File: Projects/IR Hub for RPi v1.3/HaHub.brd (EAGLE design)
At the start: 65 x 56 mm, 39 parts, among them SW1 SPST_TACT-KMR2, SW2 SPST_TACT-KMR2, SW3 SPST_TACT-KMR2, T1 2N4401, T2 2N4401, T3 2N4401, T4 2N4401

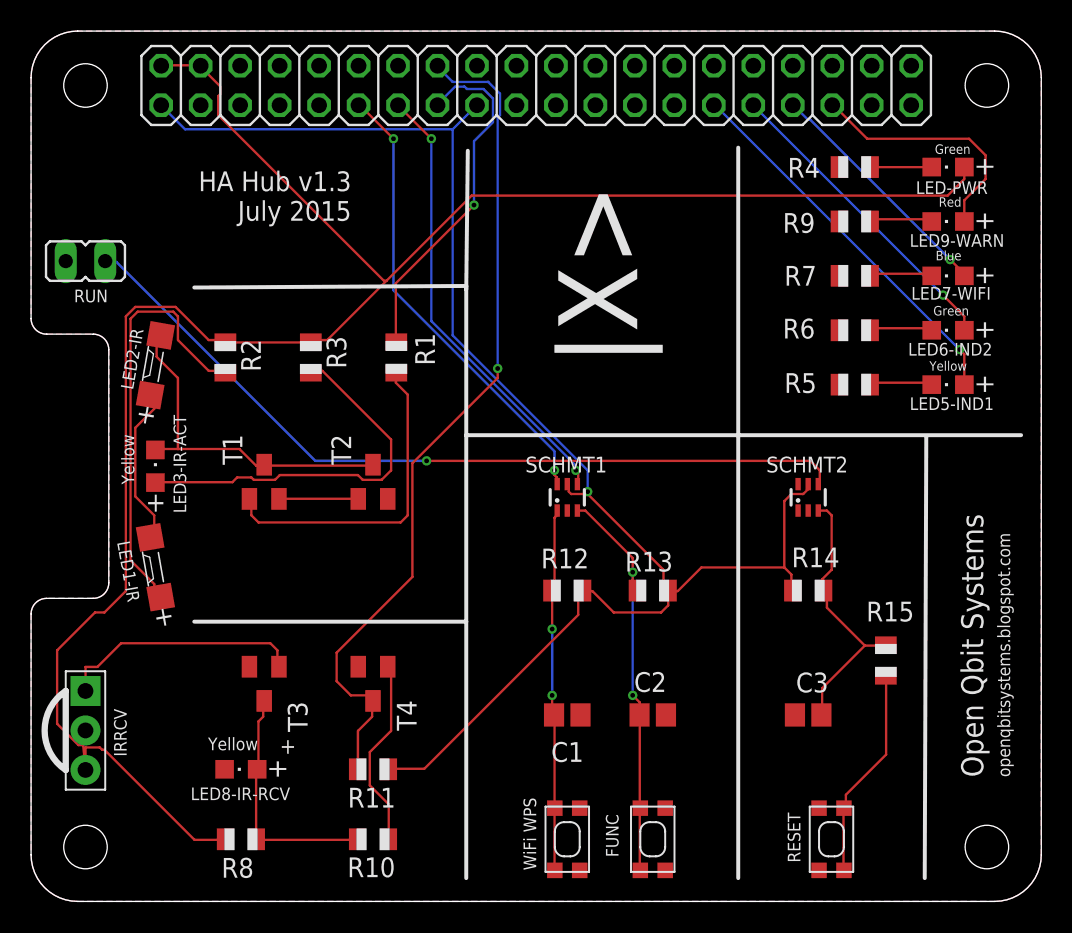
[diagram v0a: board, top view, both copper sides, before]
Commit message: Board layout changed
Removed the cutout in the board thus moved the IR emitters a bit
forward, avoiding the obstruction from the IRRCV when angled at 15deg.
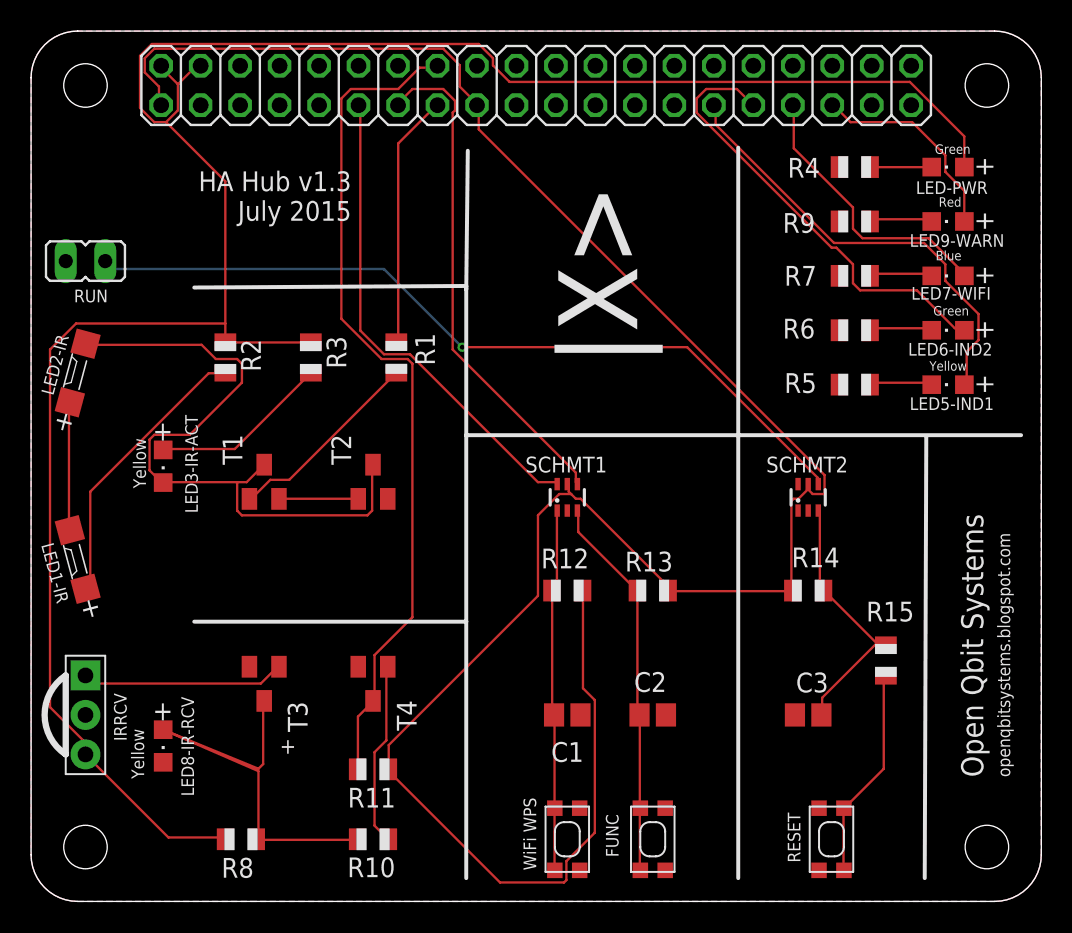
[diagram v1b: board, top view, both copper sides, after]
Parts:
- moved LED8-IR-RCV 5.22 mm to (8.50, 10.0), turned to 180 degrees
- moved LED1-IR 5.02 mm to (3.00, 22.0), turned to 195 degrees
- moved LED2-IR 5.02 mm to (3.00, 34.0), turned to 165 degrees
- moved IRRCV 1.00 mm to (3.50, 12.0)
- moved LED3-IR-ACT 0.50 mm to (8.50, 28.0), turned to 180 degrees
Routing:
- net +3V3: track 100.4 -> 146.0 mm, vias 1 -> 0
- net N$4: track 22.7 -> 43.2 mm
- net +5V: track 127.1 -> 141.4 mm
- net N$6: track 24.9 -> 11.6 mm
- net N$10: track 15.6 -> 28.8 mm
- net N$2: track 27.8 -> 18.2 mm
- net GPIO06: track 20.1 -> 29.1 mm, vias 1 -> 0
- net N$5: track 21.0 -> 12.8 mm
- net GPIO22: track 22.7 -> 16.4 mm, vias 1 -> 0
- net GPIO05: track 24.7 -> 28.9 mm, vias 1 -> 0
- net GPIO27: track 29.2 -> 32.5 mm, vias 2 -> 0
- net N$8: track 15.8 -> 13.1 mm
- net GPIO19: track 16.0 -> 13.4 mm
- net GPIO13: track 15.7 -> 18.1 mm, vias 1 -> 0
- net N$3: track 10.6 -> 8.27 mm
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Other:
- outline, holes or cut-outs redrawn
- board text added: "TODO DONE 1. Check the Schmitt debouncing on breadboard 2. Check both ICs wrt 74HC/74LV/... for 3.3V1. check the polarity of the IR LEDs 3. Add schmitt buffers for all the push buttons (create part) 4. ELIMINATED - Verify the Watchdog circuit 5. ELIMINATED - Will RPi gpio go in a state to allow disabling WD? 6. Ensure long push for RESET push button (cap and resistor values) 7. Move Power LED to 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"
- board text removed: "TODO 1. Check the Schmitt debouncing on breadboard 3. Check both ICs wrt 74HC/74LV/... for 3.3V DONE 1. check the polarity of the IR LEDs 2. Add schmitt buffers for all the push buttons (create part) 3. ELIMINATED - Verify the Watchdog circuit 4. ELIMINATED - Will RPi gpio go in a state to allow disabling WD? 5. Ensure long push for RESET push button (cap and resistor values) 6. Move Power LED to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"

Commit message: Changed v1.3 board 'via' drill size to 13mil. Plus some house keeping,
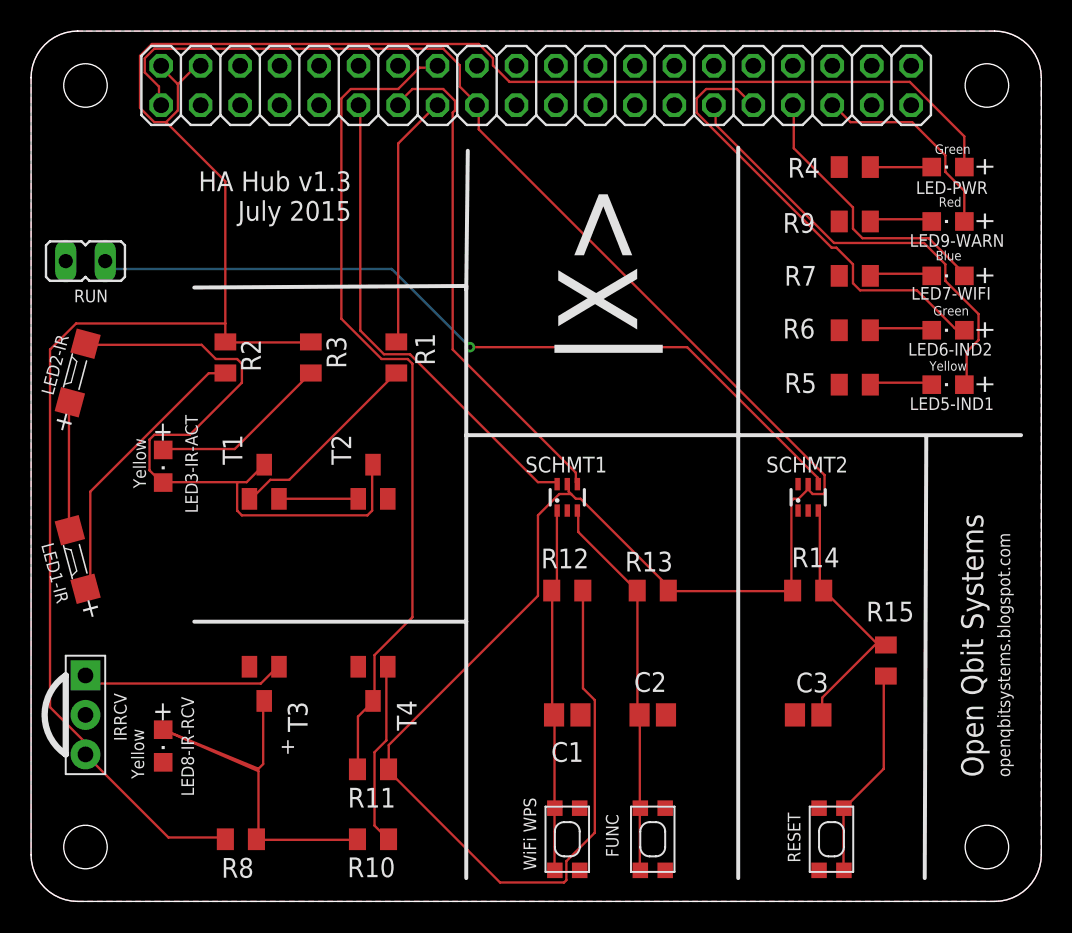
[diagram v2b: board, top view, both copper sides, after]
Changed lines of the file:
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@@
 <setting verticaltext="up"/>
 </settings>
-<grid distance="0.5" unitdist="mm" unit="mm" style="lines" multiple="1" display="yes" altdistance="0.25" altunitdist="mm" altunit="mm"/>
+<grid distance="19.6850394" unitdist="mil" unit="mil" style="lines" multiple="1" display="yes" altdistance="9.84251969" altunitdist="mil" altunit="mil"/>
 <layers>
 <layer number="1" name="Top" color="4" fill="1" visible="yes" active="yes"/>
@@
 <wire x1="45.5" y1="48.5" x2="45.5" y2="30" width="0.254" layer="25"/>
 <wire x1="63.7" y1="30" x2="28" y2="30" width="0.254" layer="25"/>
-<text x="-48.2222" y="19.964" size="1.016" layer="48">
+<text x="-4.964" y="2.7778" size="1.016" layer="48" rot="R90">
 TODO
 DONE
@@
 <text x="63" y="8" size="0.8128" layer="25" rot="R90">openqbitsystems.blogspot.com</text>
 <text x="60" y="42" size="2.1844" layer="26" rot="MR0">Home Automation Hub v1.3</text>
+<text x="46" y="28" size="5.08" layer="26" rot="MR0">|X&gt;</text>
 </plain>
 <attributes>
@@
 </class>
 </classes>
-<designrules name="ITEADstudio_DRC">
+<designrules name="OSHParkDesignRules *">
 <description language="de">&lt;b&gt;EAGLE Design Rules&lt;/b&gt;
 &lt;p&gt;
@@
 Einstellungen hier und speichern die Design Rules unter
 einem neuen Namen ab.</description>
-<description language="en">&lt;b&gt;EAGLE Design Rules&lt;/b&gt;
+<description language="en">&lt;b&gt;Laen's PCB Order Design Rules&lt;/b&gt;
 &lt;p&gt;
-The default Design Rules have been set to cover
-a wide range of applications. Your particular design
-may have different requirements, so please make the
-necessary adjustments and save your customized
-design rules under a new name.</description>
-<description language="zh">&lt;b&gt;Seeed Studio EAGLE Design Rules&lt;/b&gt;
-</description>
+Please make sure your boards conform to these design rules.</description>
 <param name="layerSetup" value="(1*16)"/>
-<param name="mtCopper" value="0.035mm 0.035mm 0.035mm 0.035mm 0.035mm 0.035mm 0.035mm 0.035mm 0.035mm 0.035mm 0.035mm 0.035mm 0.035mm 0.035mm 0.035mm 0.035mm"/>
-<param name="mtIsolate" value="1.5mm 0.15mm 0.2mm 0.15mm 0.2mm 0.15mm 0.2mm 0.15mm 0.2mm 0.15mm 0.2mm 0.15mm 0.2mm 0.15mm 0.2mm"/>
+<param name="mtCopper" value="0.0356mm 0.0356mm 0.0356mm 0.0356mm 0.0356mm 0.0356mm 0.0356mm 0.0356mm 0.0356mm 0.0356mm 0.0356mm 0.0356mm 0.0356mm 0.0356mm 0.0356mm 0.0356mm"/>
+<param name="mtIsolate" value="1.5011mm 0.1499mm 0.2007mm 0.1499mm 0.2007mm 0.1499mm 0.2007mm 0.1499mm 0.2007mm 0.1499mm 0.2007mm 0.1499mm 0.2007mm 0.1499mm 0.2007mm"/>
 <param name="mdWireWire" value="6mil"/>
 <param name="mdWirePad" value="6mil"/>
@@
 <param name="mdPadVia" value="6mil"/>
 <param name="mdViaVia" value="6mil"/>
-<param name="mdSmdPad" value="0mil"/>
-<param name="mdSmdVia" value="0mil"/>
-<param name="mdSmdSmd" value="0mil"/>
+<param name="mdSmdPad" value="6mil"/>
+<param name="mdSmdVia" value="6mil"/>
+<param name="mdSmdSmd" value="6mil"/>
 <param name="mdViaViaSameLayer" value="8mil"/>
 <param name="mnLayersViaInSmd" value="2"/>
-<param name="mdCopperDimension" value="10mil"/>
-<param name="mdDrill" value="10mil"/>
+<param name="mdCopperDimension" value="15mil"/>
+<param name="mdDrill" value="6mil"/>
 <param name="mdSmdStop" value="0mil"/>
 <param name="msWidth" value="6mil"/>
-<param name="msDrill" value="12mil"/>
-<param name="msMicroVia" value="12mil"/>
+<param name="msDrill" value="13mil"/>
+<param name="msMicroVia" value="13mil"/>
 <param name="msBlindViaRatio" value="0.5"/>
 <param name="rvPadTop" value="0.25"/>
@@
 <param name="rvMicroViaOuter" value="0.25"/>
 <param name="rvMicroViaInner" value="0.25"/>
-<param name="rlMinPadTop" value="10mil"/>
+<param name="rlMinPadTop" value="7mil"/>
 <param name="rlMaxPadTop" value="20mil"/>
-<param name="rlMinPadInner" value="10mil"/>
+<param name="rlMinPadInner" value="7mil"/>
 <param name="rlMaxPadInner" value="20mil"/>
-<param name="rlMinPadBottom" value="10mil"/>
+<param name="rlMinPadBottom" value="7mil"/>
 <param name="rlMaxPadBottom" value="20mil"/>
-<param name="rlMinViaOuter" value="6mil"/>
+<param name="rlMinViaOuter" value="7mil"/>
 <param name="rlMaxViaOuter" value="20mil"/>
-<param name="rlMinViaInner" value="6mil"/>
+<param name="rlMinViaInner" value="7mil"/>
 <param name="rlMaxViaInner" value="20mil"/>
 <param name="rlMinMicroViaOuter" value="4mil"/>
@@
 <param name="psTop" value="-1"/>
 <param name="psBottom" value="-1"/>
-<param name="psFirst" value="0"/>
+<param name="psFirst" value="-1"/>
 <param name="psElongationLong" value="100"/>
 <param name="psElongationOffset" value="100"/>
 <param name="mvStopFrame" value="1"/>
 <param name="mvCreamFrame" value="0"/>
-<param name="mlMinStopFrame" value="2mil"/>
-<param name="mlMaxStopFrame" value="2mil"/>
+<param name="mlMinStopFrame" value="3mil"/>
+<param name="mlMaxStopFrame" value="3mil"/>
 <param name="mlMinCreamFrame" value="0mil"/>
 <param name="mlMaxCreamFrame" value="0mil"/>
@@
 <param name="checkAngle" value="0"/>
 <param name="checkFont" value="1"/>
-<param name="checkRestrict" value="0"/>
+<param name="checkRestrict" value="1"/>
 <param name="useDiameter" value="13"/>
 <param name="maxErrors" value="50"/>
@@
 <wire x1="50.5968" y1="27.2796" x2="50.5968" y2="26.9748" width="0.1524" layer="1"/>
 <wire x1="42.2148" y1="35.6616" x2="50.5968" y2="27.2796" width="0.1524" layer="1"/>
-<wire x1="27.7368" y1="35.6616" x2="42.2148" y2="35.6616" width="0.1524" layer="1"/>
-<wire x1="22.7076" y1="40.6908" x2="27.7368" y2="35.6616" width="0.1524" layer="16"/>
-<wire x1="5.334" y1="40.6908" x2="22.7076" y2="40.6908" width="0.1524" layer="16"/>
+<wire x1="28.2368" y1="35.6616" x2="42.2148" y2="35.6616" width="0.1524" layer="1"/>
+<wire x1="23.2076" y1="40.6908" x2="28.2368" y2="35.6616" width="0.1524" layer="16"/>
+<wire x1="5.334" y1="40.6908" x2="23.2076" y2="40.6908" width="0.1524" layer="16"/>
 <wire x1="4.8768" y1="41.148" x2="5.334" y2="40.6908" width="0.1524" layer="16"/>
 <wire x1="50.5968" y1="26.9748" x2="50.65" y2="26.85" width="0.1524" layer="1"/>
 <wire x1="4.8768" y1="41.148" x2="4.77" y2="41.2" width="0.1524" layer="16"/>
-<via x="27.7368" y="35.6616" extent="1-16" drill="0.3048"/>
+<via x="28.2368" y="35.6616" extent="1-16" drill="0.3302"/>
 </signal>
 <signal name="N$1">
